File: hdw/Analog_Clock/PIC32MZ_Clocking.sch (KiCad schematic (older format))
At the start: 14 parts

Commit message: More schematic work
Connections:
- net MCU_POSC renamed PIC32MZ_POSC
- net MCU_SOSC renamed PIC32MZ_SOSC
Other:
- note added: "32.768kHz"
- note added: "8MHz"
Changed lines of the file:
@@
 EESchema Schematic File Version 4
+LIBS:Analog_Clock-cache
 EELAYER 30 0
 EELAYER END
@@
 $EndComp
 Text GLabel 6180 2610 2    50   Output ~ 0
-MCU_POSC
+PIC32MZ_POSC
 $Comp
 L Custom_Library:R_Custom R?
@@
 $EndComp
 Text GLabel 6180 5100 2    50   Output ~ 0
-MCU_SOSC
+PIC32MZ_SOSC
 $Comp
 L Custom_Library:R_Custom R?
@@
 Wire Wire Line
 	4880 2150 4880 2310
+Text Notes 6370 2910 0    50   ~ 0
+8MHz
+Text Notes 6370 5360 0    50   ~ 0
+32.768kHz
 $EndSCHEMATC

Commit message: a few sch adjustments
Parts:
- removed C?: 0.1uF, Capacitors_SMD:C_0402, symbol Custom_Library:C_Custom
- removed C?: 1nF, Capacitors_SMD:C_0402, symbol Custom_Library:C_Custom
- removed C?: 10nF, Capacitors_SMD:C_0402, symbol Custom_Library:C_Custom
- removed L?: 600R 0.5A, Inductors_SMD:L_0402, symbol Device:Ferrite_Bead
- removed R?: 10k, Resistors_SMD:R_0402, symbol Custom_Library:R_Custom
- removed R?: 100, Resistors_SMD:R_0402, symbol Custom_Library:R_Custom
- removed X?: ECS-327KE, Custom Footprints Library:ECS-327KE, symbol Custom_Library:ECS-327KE
- added R? (x2): 10k, Resistors_SMD:R_0402, symbol Custom_Library:R_Custom
- added TP?: TP, Custom Footprints Library:Test_Point, symbol Custom_Library:TP
- R?: Digi-Key PN (none) -> 541-100LCT-ND
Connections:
- net GND: now also R?.2, R?.2
- net at C?.1, C?.1, C?.1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: no longer X?.1 (EN)
- net PIC32MZ_POSC renamed PIC32MZ_POSC_EC
- new net PIC32MZ_POSC_EC_Enable: R?.1, X?.1 (EN)
- new net PIC32MZ_REFCLK1: R?.1, TP?.1 (TP)
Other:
- note removed: "32.768kHz"
- note removed: "8MHz"
- moved on the sheet: C?, L?, R?, X?

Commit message: more sch progress
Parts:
- added C?: 0.1uF, Capacitors_SMD:C_0402, symbol Custom_Library:C_Custom
- added C?: 1nF, Capacitors_SMD:C_0402, symbol Custom_Library:C_Custom
- added C?: 10nF, Capacitors_SMD:C_0402, symbol Custom_Library:C_Custom
- added L?: 600R 0.5A, Inductors_SMD:L_0402, symbol Device:Ferrite_Bead
- added R?: 10k, Resistors_SMD:R_0402, symbol Custom_Library:R_Custom
- added R?: 100, Resistors_SMD:R_0402, symbol Custom_Library:R_Custom
- added X?: ECS-327KE, Custom Footprints Library:ECS-327KE, symbol Custom_Library:ECS-327KE
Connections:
- net +3V3: now also L?.2
- net GND: now also C?.2, C?.2, C?.2, R?.2, X?.2 (GND)
- new net: R?.1, X?.3 (OUT)
- new net: C?.1, C?.1, C?.1, L?.1, X?.1 (EN), X?.4 (Vdd)
- new net PIC32MZ_SOSC: R?.1, R?.2

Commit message: more analog work, added some more sch stuff
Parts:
- added R?: 10k, Resistors_SMD:R_0402, symbol Custom_Library:R_Custom
- added TP?: TP, Custom Footprints Library:Test_Point, symbol Custom_Library:TP
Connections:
- net GND: now also R?.2
- new net PIC32MZ_RTCC_CLK: R?.1, TP?.1 (TP)
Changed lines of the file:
@@
 $Descr A 11000 8500
 encoding utf-8
-Sheet 11 23
+Sheet 11 24
 Title "Pulse Oximeter"
 Date "2020-08-01"
@@
 Wire Wire Line
 	5510 4750 5510 4830
+Text GLabel 2680 4220 0    50   Input ~ 0
+PIC32MZ_RTCC_CLK
+$Comp
+L Custom_Library:R_Custom R?
+U 1 1 5F3B80FA
+P 2760 4450
+AR Path="/5BAAE1F3/5F3B80FA" Ref="R?"  Part="1"
+AR Path="/5BAAE1DC/5F3B80FA" Ref="R?"  Part="1"
+AR Path="/5BAAE16C/5F3B80FA" Ref="R?"  Part="1"
+AR Path="/5BB844FD/5F3B80FA" Ref="R?"  Part="1"
+AR Path="/5BF346B3/5F3B80FA" Ref="R?"  Part="1"
+AR Path="/5CAD2D97/5F3B80FA" Ref="R?"  Part="1"
+AR Path="/5CB7A8BC/5F3B80FA" Ref="R?"  Part="1"
+AR Path="/5E01BCC3/5F3B80FA" Ref="R?"  Part="1"
+AR Path="/5E697952/5F3B80FA" Ref="R?"  Part="1"
+AR Path="/5EAE2F15/5F3B80FA" Ref="R?"  Part="1"
+AR Path="/5E939EDE/5F3B80FA" Ref="R?"  Part="1"
+F 0 "R?" H 2700 4450 50  0000 R CNN
+F 1 "10k" V 2760 4450 50  0000 C CNN
+F 2 "Resistors_SMD:R_0402" H 2760 4450 50  0001 C CNN
+F 3 "" H 2760 4450 50  0001 C CNN
+F 4 "0402" H 2830 4530 50  0000 L CNN "display_footprint"
+F 5 "1%" H 2830 4450 50  0000 L CNN "Tolerance"
+F 6 "1/16W" H 2830 4380 50  0000 L CNN "Wattage"
+F 7 "RMCF0402FT10K0CT-ND" H 2760 4450 50  0001 C CNN "Digi-Key PN"
+	1    2760 4450
+	-1   0    0    -1
+$EndComp
+$Comp
+L power:GND #PWR?
+U 1 1 5F3B8104
+P 2760 4600
+F 0 "#PWR?" H 2760 4350 50  0001 C CNN
+F 1 "GND" H 2760 4450 50  0000 C CNN
+F 2 "" H 2760 4600 50  0001 C CNN
+F 3 "" H 2760 4600 50  0001 C CNN
+	1    2760 4600
+	1    0    0    -1
+$EndComp
+Wire Wire Line
+	2760 4300 2760 4220
+Wire Wire Line
+	2760 4220 2680 4220
+$Comp
+L Custom_Library:TP TP?
+U 1 1 5F3B8110
+P 2840 4220
+AR Path="/5C1D5CD8/5F3B8110" Ref="TP?"  Part="1"
+AR Path="/5C1D5C9E/5F3B8110" Ref="TP?"  Part="1"
+AR Path="/5CB6F1ED/5F3B8110" Ref="TP?"  Part="1"
+AR Path="/5E939CFF/5F3B8110" Ref="TP?"  Part="1"
+AR Path="/5E9E0E87/5F3B8110" Ref="TP?"  Part="1"
+AR Path="/5EAE2D66/5F3B8110" Ref="TP?"  Part="1"
+AR Path="/5EAE2F15/5F3B8110" Ref="TP?"  Part="1"
+AR Path="/5E939EDE/5F3B8110" Ref="TP?"  Part="1"
+F 0 "TP?" V 2840 4370 50  0000 L CNN
+F 1 "TP" H 2840 4370 50  0001 C CNN
+F 2 "Custom Footprints Library:Test_Point" H 2840 4220 60  0001 C CNN
+F 3 "" H 2840 4220 60  0000 C CNN
+	1    2840 4220
+	0    1    1    0
+$EndComp
+Wire Wire Line
+	2840 4220 2760 4220
+Connection ~ 2760 4220
 $EndSCHEMATC

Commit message: big sch push
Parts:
- C1101, C1102: renamed from C?; footprint Capacitors_SMD:C_0402 -> Capacitors_SMD:C_0603; Digi-Key PN 490-10701-1-ND -> 399-7845-1-ND; display_footprint 0402 -> 0603
- C1103, C1104: renamed from C?; footprint Capacitors_SMD:C_0402 -> Capacitors_SMD:C_0603; Digi-Key PN 490-13295-1-ND -> 399-7842-1-ND; display_footprint 0402 -> 0603
- C1105, C1106: renamed from C?; footprint Capacitors_SMD:C_0402 -> Capacitors_SMD:C_0603; Digi-Key PN 399-1032-1-ND -> 399-1083-1-ND; display_footprint 0402 -> 0603
- L1101, L1102: renamed from L?; footprint Inductors_SMD:L_0402 -> Inductors_SMD:L_0603; Digi-Key PN 490-5441-1-ND -> 732-1593-1-ND
- R1101, R1102, R1103, R1106, R1107: renamed from R?; footprint Resistors_SMD:R_0402 -> Resistors_SMD:R_0603; Digi-Key PN RMCF0402FT10K0CT-ND -> (none); Wattage 1/16W -> 1/10W; display_footprint 0402 -> 0603
- R1104, R1105: renamed from R?; footprint Resistors_SMD:R_0402 -> Resistors_SMD:R_0603; Digi-Key PN 541-100LCT-ND -> (none); Wattage 1/16W -> 1/10W; display_footprint 0402 -> 0603
- gave numbers to parts that had none: 4

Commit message: Much more schematic progress
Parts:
- R1101, R1102, R1103, R1106, R1107: Digi-Key PN (none) -> YAG2321CT-ND
- R1104, R1105: Digi-Key PN (none) -> RMCF0603FT100RCT-ND
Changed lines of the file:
@@
 encoding utf-8
 Sheet 11 25
-Title "Pulse Oximeter"
-Date "2020-08-01"
+Title "Analog Clock"
+Date "2020-08-15"
 Rev "A"
 Comp "Drew Maatman"
@@
 F 5 "1%" H 6630 2930 50  0000 L CNN "Tolerance"
 F 6 "1/10W" H 6630 2860 50  0000 L CNN "Wattage"
-F 7 "" H 6560 2930 50  0001 C CNN "Digi-Key PN"
+F 7 "YAG2321CT-ND" H 6560 2930 50  0001 C CNN "Digi-Key PN"
 	1    6560 2930
 	-1   0    0    -1
@@
 F 5 "1%" V 6310 2700 50  0001 C CNN "Tolerance"
 F 6 "1/10W" V 6410 2700 50  0001 C CNN "Wattage"
-F 7 "" H 6410 3100 60  0001 C CNN "Digi-Key PN"
+F 7 "RMCF0603FT100RCT-ND" H 6410 3100 60  0001 C CNN "Digi-Key PN"
 	1    6110 2700
 	0    -1   1    0
@@
 F 5 "1%" H 5030 2930 50  0000 L CNN "Tolerance"
 F 6 "1/10W" H 5030 2860 50  0000 L CNN "Wattage"
-F 7 "" H 4960 2930 50  0001 C CNN "Digi-Key PN"
+F 7 "YAG2321CT-ND" H 4960 2930 50  0001 C CNN "Digi-Key PN"
 	1    4960 2930
 	-1   0    0    -1
@@
 F 5 "1%" H 2830 5360 50  0000 L CNN "Tolerance"
 F 6 "1/10W" H 2830 5290 50  0000 L CNN "Wattage"
-F 7 "" H 2760 5360 50  0001 C CNN "Digi-Key PN"
+F 7 "YAG2321CT-ND" H 2760 5360 50  0001 C CNN "Digi-Key PN"
 	1    2760 5360
 	-1   0    0    -1
@@
 F 5 "1%" H 6630 5360 50  0000 L CNN "Tolerance"
 F 6 "1/10W" H 6630 5290 50  0000 L CNN "Wattage"
-F 7 "" H 6560 5360 50  0001 C CNN "Digi-Key PN"
+F 7 "YAG2321CT-ND" H 6560 5360 50  0001 C CNN "Digi-Key PN"
 	1    6560 5360
 	-1   0    0    -1
@@
 F 5 "1%" V 6310 5130 50  0001 C CNN "Tolerance"
 F 6 "1/10W" V 6410 5130 50  0001 C CNN "Wattage"
-F 7 "" H 6410 5530 60  0001 C CNN "Digi-Key PN"
+F 7 "RMCF0603FT100RCT-ND" H 6410 5530 60  0001 C CNN "Digi-Key PN"
 	1    6110 5130
 	0    -1   1    0
@@
 F 5 "1%" H 2830 4450 50  0000 L CNN "Tolerance"
 F 6 "1/10W" H 2830 4380 50  0000 L CNN "Wattage"
-F 7 "" H 2760 4450 50  0001 C CNN "Digi-Key PN"
+F 7 "YAG2321CT-ND" H 2760 4450 50  0001 C CNN "Digi-Key PN"
 	1    2760 4450
 	-1   0    0    -1

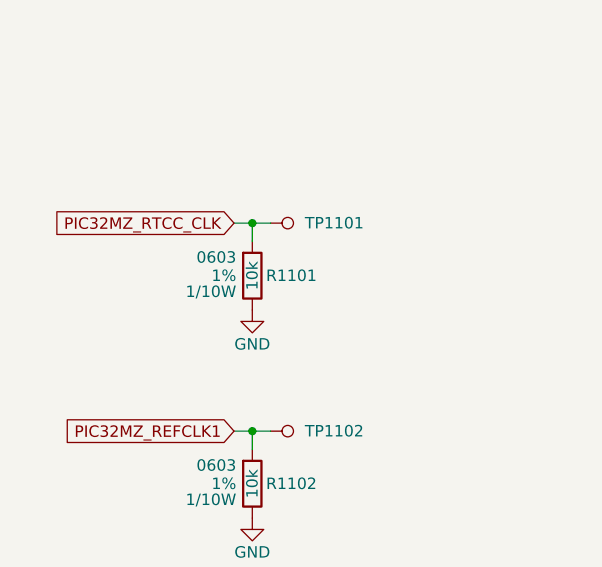
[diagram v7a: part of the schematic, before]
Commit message: Arranged more components on PCB
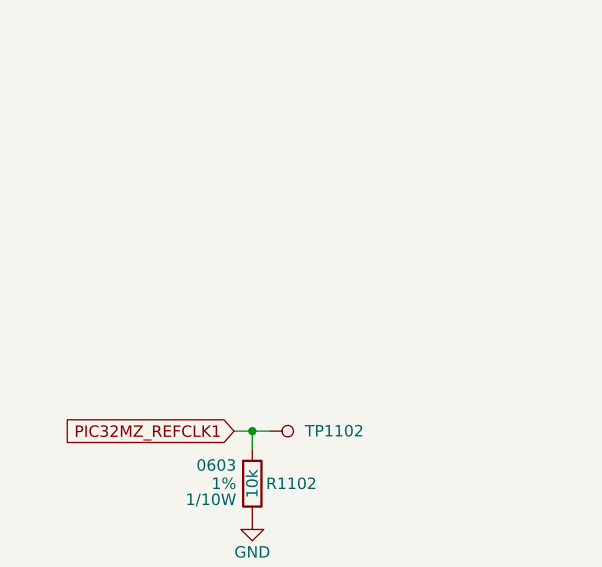
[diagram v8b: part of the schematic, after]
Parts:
- removed R1101: 10k, Resistors_SMD:R_0603, symbol Custom_Library:R_Custom
- removed TP1101: TP, Custom Footprints Library:Test_Point, symbol Custom_Library:TP
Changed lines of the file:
@@
 Wire Wire Line
 	5510 4750 5510 4830
-Text GLabel 2680 4220 0    50   Input ~ 0
-PIC32MZ_RTCC_CLK
-$Comp
-L Custom_Library:R_Custom R?
-U 1 1 5F3B80FA
-P 2760 4450
-AR Path="/5BAAE1F3/5F3B80FA" Ref="R?"  Part="1"
-AR Path="/5BAAE1DC/5F3B80FA" Ref="R?"  Part="1"
-AR Path="/5BAAE16C/5F3B80FA" Ref="R?"  Part="1"
-AR Path="/5BB844FD/5F3B80FA" Ref="R?"  Part="1"
-AR Path="/5BF346B3/5F3B80FA" Ref="R?"  Part="1"
-AR Path="/5CAD2D97/5F3B80FA" Ref="R?"  Part="1"
-AR Path="/5CB7A8BC/5F3B80FA" Ref="R?"  Part="1"
-AR Path="/5E01BCC3/5F3B80FA" Ref="R?"  Part="1"
-AR Path="/5E697952/5F3B80FA" Ref="R?"  Part="1"
-AR Path="/5EAE2F15/5F3B80FA" Ref="R?"  Part="1"
-AR Path="/5E939EDE/5F3B80FA" Ref="R1101"  Part="1"
-F 0 "R1101" H 2700 4450 50  0000 R CNN
-F 1 "10k" V 2760 4450 50  0000 C CNN
-F 2 "Resistors_SMD:R_0603" H 2760 4450 50  0001 C CNN
-F 3 "" H 2760 4450 50  0001 C CNN
-F 4 "0603" H 2830 4530 50  0000 L CNN "display_footprint"
-F 5 "1%" H 2830 4450 50  0000 L CNN "Tolerance"
-F 6 "1/10W" H 2830 4380 50  0000 L CNN "Wattage"
-F 7 "YAG2321CT-ND" H 2760 4450 50  0001 C CNN "Digi-Key PN"
-	1    2760 4450
-	-1   0    0    -1
-$EndComp
-$Comp
-L power:GND #PWR01101
-U 1 1 5F3B8104
-P 2760 4600
-F 0 "#PWR01101" H 2760 4350 50  0001 C CNN
-F 1 "GND" H 2760 4450 50  0000 C CNN
-F 2 "" H 2760 4600 50  0001 C CNN
-F 3 "" H 2760 4600 50  0001 C CNN
-	1    2760 4600
-	1    0    0    -1
-$EndComp
-Wire Wire Line
-	2760 4300 2760 4220
-Wire Wire Line
-	2760 4220 2680 4220
-$Comp
-L Custom_Library:TP TP?
-U 1 1 5F3B8110
-P 2840 4220
-AR Path="/5C1D5CD8/5F3B8110" Ref="TP?"  Part="1"
-AR Path="/5C1D5C9E/5F3B8110" Ref="TP?"  Part="1"
-AR Path="/5CB6F1ED/5F3B8110" Ref="TP?"  Part="1"
-AR Path="/5E939CFF/5F3B8110" Ref="TP?"  Part="1"
-AR Path="/5E9E0E87/5F3B8110" Ref="TP?"  Part="1"
-AR Path="/5EAE2D66/5F3B8110" Ref="TP?"  Part="1"
-AR Path="/5EAE2F15/5F3B8110" Ref="TP?"  Part="1"
-AR Path="/5E939EDE/5F3B8110" Ref="TP1101"  Part="1"
-F 0 "TP1101" V 2840 4370 50  0000 L CNN
-F 1 "TP" H 2840 4370 50  0001 C CNN
-F 2 "Custom Footprints Library:Test_Point" H 2840 4220 60  0001 C CNN
-F 3 "" H 2840 4220 60  0000 C CNN
-	1    2840 4220
-	0    1    1    0
-$EndComp
-Wire Wire Line
-	2840 4220 2760 4220
-Connection ~ 2760 4220
 $EndSCHEMATC
